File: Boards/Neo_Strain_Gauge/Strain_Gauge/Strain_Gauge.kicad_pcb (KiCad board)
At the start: 2 copper layers, 85 x 56 mm, 60 parts, among them J1 Screw_Terminal_01x03, J2 Screw_Terminal_01x03, J3 Screw_Terminal_01x03, J4 Screw_Terminal_01x03, J5 Conn_01x02, J6 USB_B_Micro, J7 Conn_02x10_Counter_Clockwise, J8 Conn_02x12_Counter_Clockwise, U1 W25Q128JVS, U2 NCP1117-3.3_SOT223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

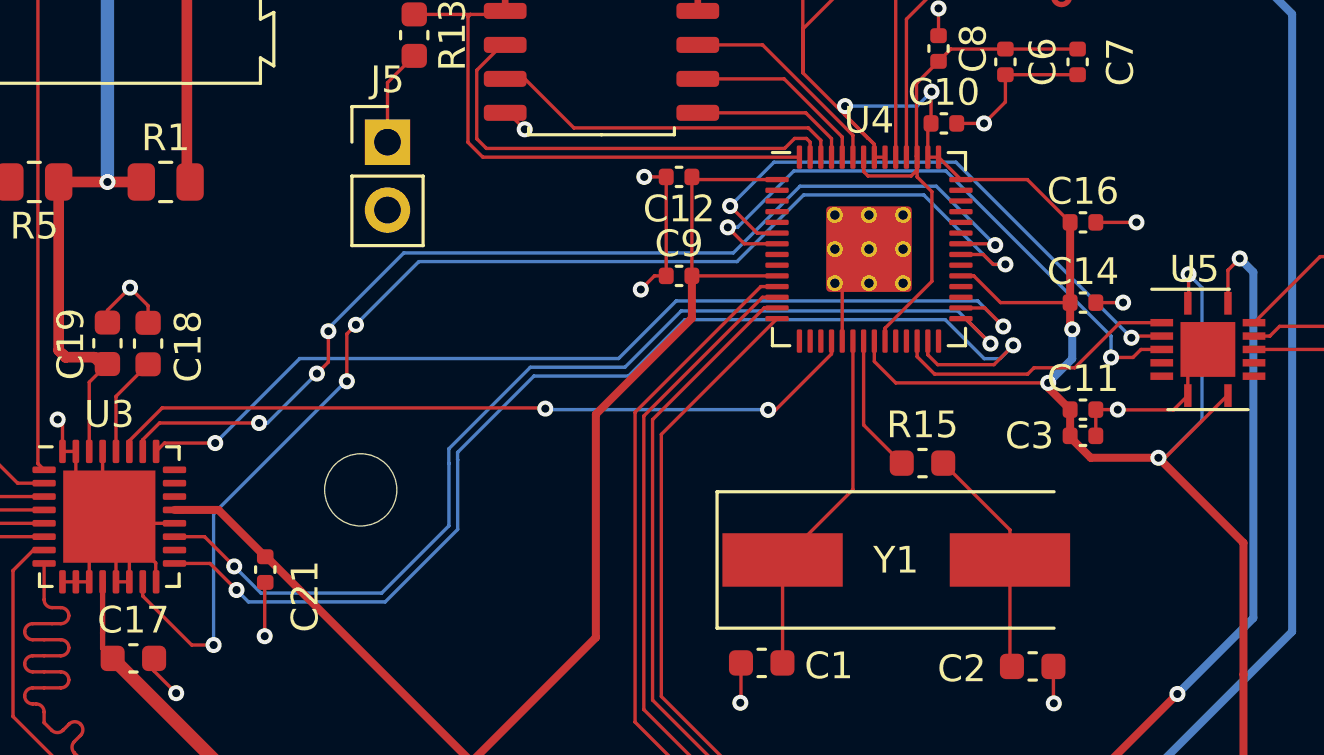
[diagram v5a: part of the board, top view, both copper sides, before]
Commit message: Swap what we use for the SPI pins to make routing slightly better
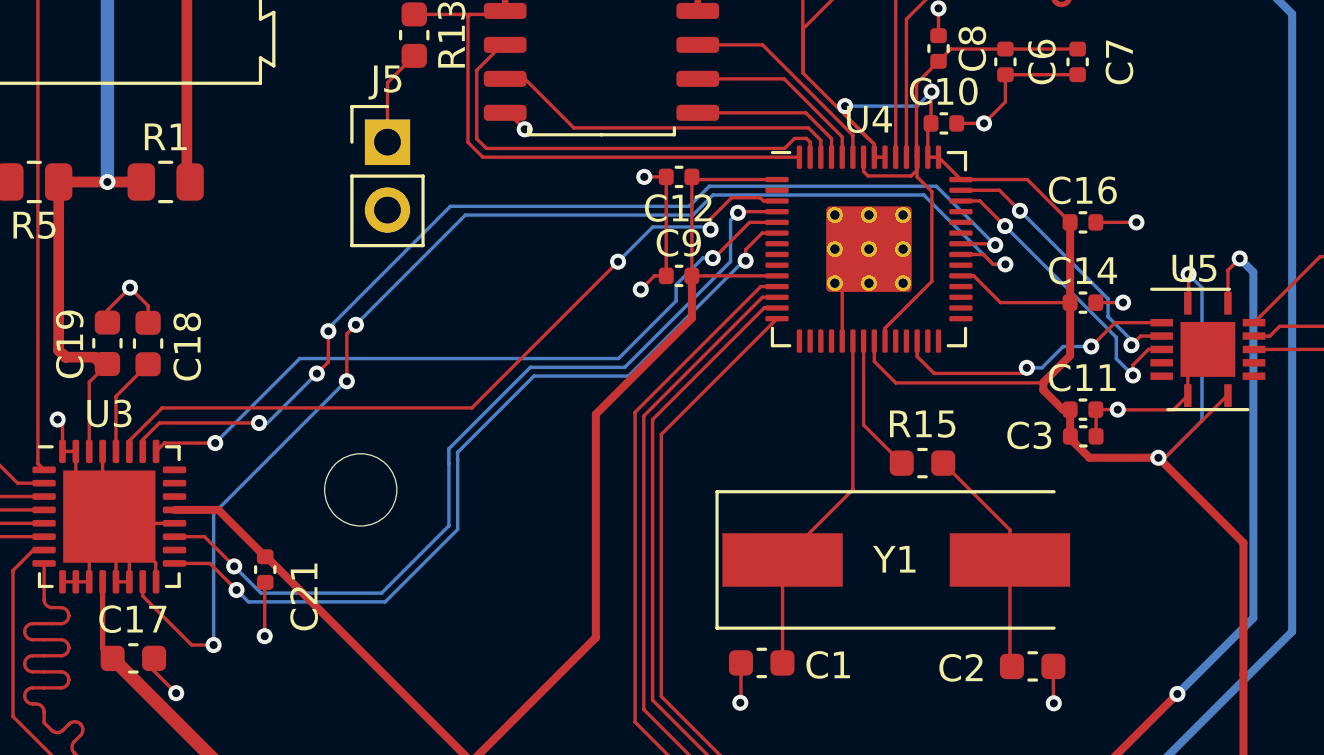
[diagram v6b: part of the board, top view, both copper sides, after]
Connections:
- U3 pad 17: /GPIO16 -> /GPIO4
- U3 pad 19: /GPIO18 -> /GPIO2
- U3 pad 25: /GPIO19 -> /GPIO3
- U3 pad 27: /GPIO15 -> /GPIO1
- U5 pad 3: /GPIO4 -> /GPIO29_ADC3
- U5 pad 4: /GPIO5 -> /GPIO28_ADC2
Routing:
- net /GPIO16: track 43.0 -> 0.00 mm, vias 2 -> 0
- net /GPIO18: track 39.4 -> 0.00 mm, vias 2 -> 0
- net /GPIO19: track 36.3 -> 0.00 mm, vias 2 -> 0
- net /GPIO2: track 0.00 -> 31.9 mm, vias 0 -> 2
- net /GPIO1: track 0.00 -> 28.8 mm, vias 0 -> 2
- net /GPIO15: track 28.5 -> 0.00 mm, vias 2 -> 0
- net /GPIO3: track 0.00 -> 27.1 mm, vias 0 -> 2
- net /GPIO5: track 22.7 -> 0.00 mm, vias 2 -> 0
- net /GPIO28_ADC2: track 0.00 -> 11.3 mm, vias 0 -> 2
- net /GPIO29_ADC3: track 0.00 -> 10.6 mm, vias 0 -> 2
- net /GPIO4: track 21.7 -> 30.8 mm
- net +3V3: track 192.2 -> 192.3 mm, vias 8 -> 6
- net /RUN: vias 0 -> 2

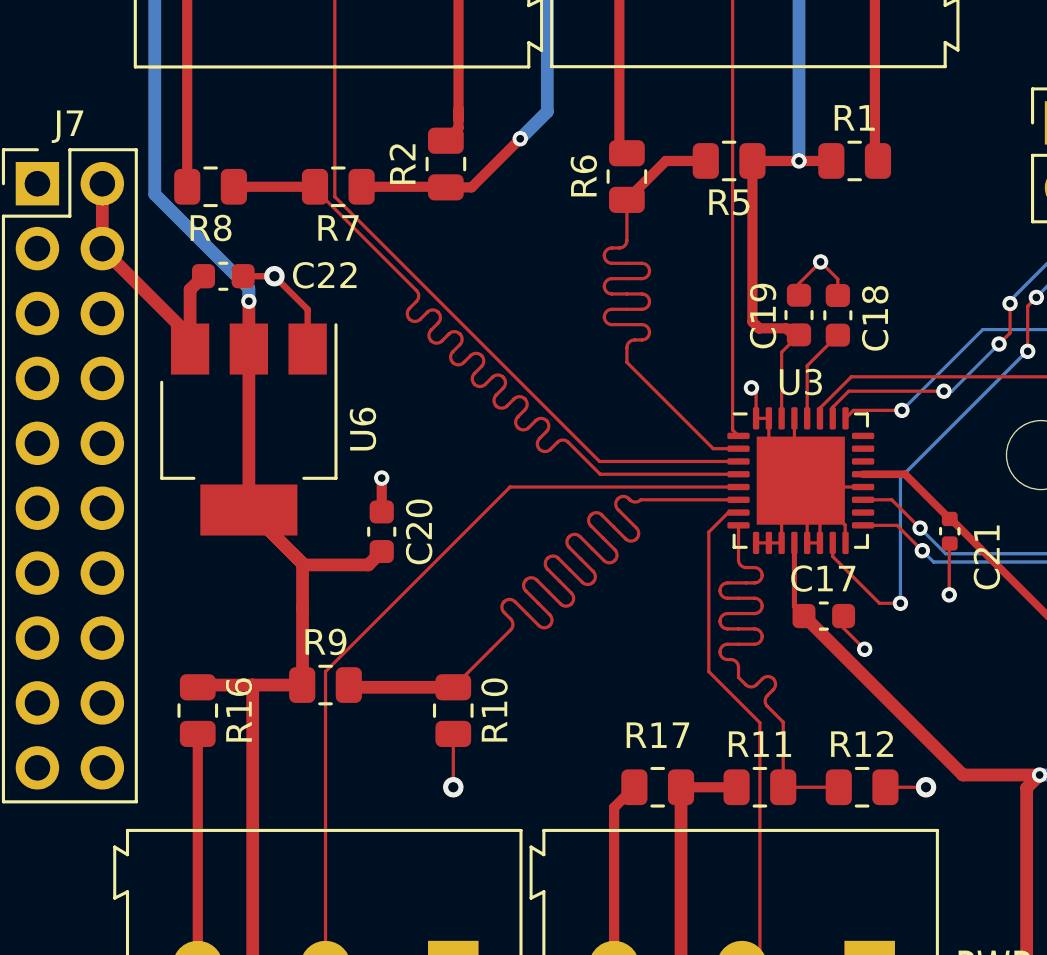
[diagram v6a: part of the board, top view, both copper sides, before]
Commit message: Filter the voltage input to the system
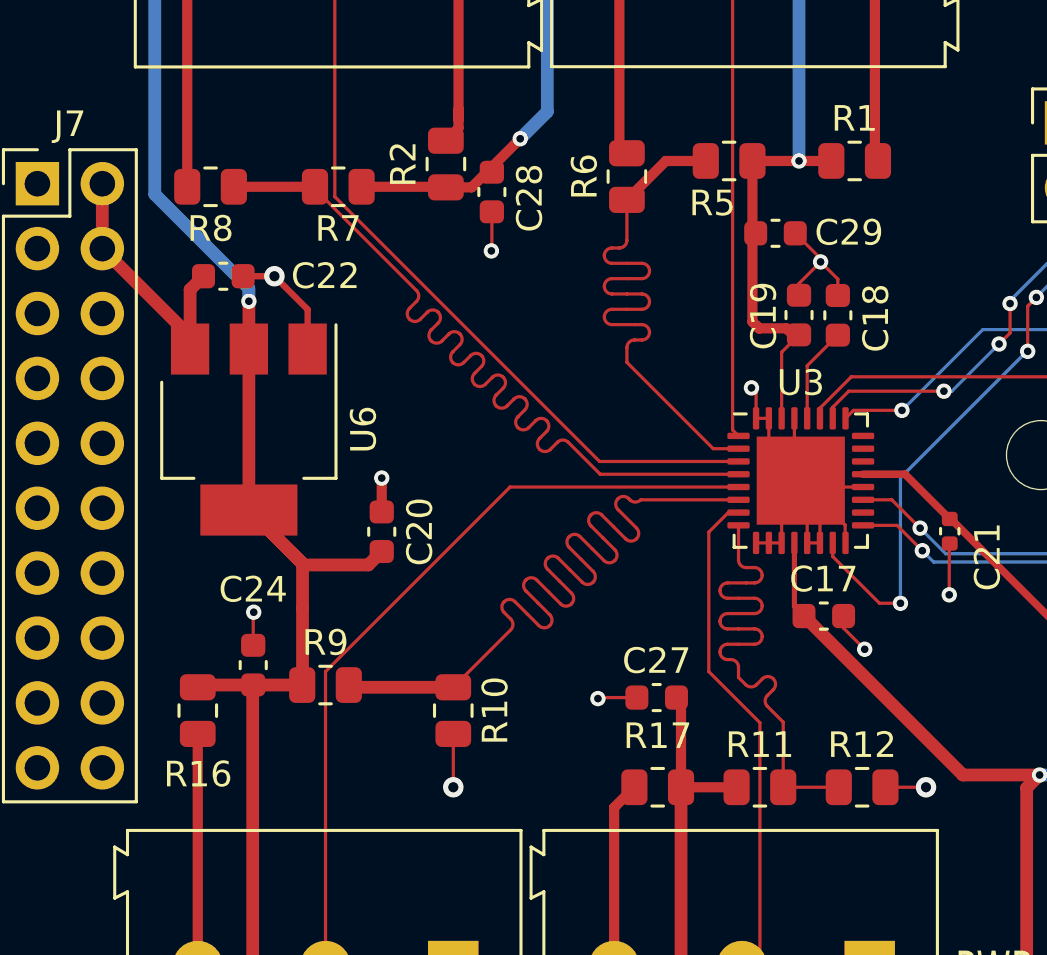
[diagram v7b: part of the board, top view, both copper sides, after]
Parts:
- added C24: 0.1pF, Capacitor_SMD:C_0603_1608Metric, F.Cu at (111.2, 90.2)
- added C27: 0.1pF, Capacitor_SMD:C_0603_1608Metric, F.Cu at (127.0, 91.5)
- added C28: 0.1pF, Capacitor_SMD:C_0603_1608Metric, F.Cu at (120.5, 71.7)
- added C29: 0.1pF, Capacitor_SMD:C_0603_1608Metric, F.Cu at (131.6, 73.3)
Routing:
- net GND: track 110.0 -> 115.9 mm, vias 21 -> 24
- net +5V: track 224.2 -> 227.7 mm

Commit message: Add test points to debug board communication
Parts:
- added TP1: TestPoint, TestPoint:TestPoint_THTPad_D1.0mm_Drill0.5mm, F.Cu at (147.6, 76.4)
- added TP2: TestPoint, TestPoint:TestPoint_THTPad_D1.0mm_Drill0.5mm, F.Cu at (138.3, 76.5)
- added TP3: TestPoint, TestPoint:TestPoint_THTPad_D1.0mm_Drill0.5mm, F.Cu at (144.6, 76.4)
- added TP4: TestPoint, TestPoint:TestPoint_THTPad_D1.0mm_Drill0.5mm, F.Cu at (147.5, 83.8)
- added TP5: TestPoint, TestPoint:TestPoint_THTPad_D1.0mm_Drill0.5mm, F.Cu at (149.2, 80.0)
- added TP6: TestPoint, TestPoint:TestPoint_THTPad_D1.0mm_Drill0.5mm, F.Cu at (170.9, 83.2)
- added TP7: TestPoint, TestPoint:TestPoint_THTPad_D1.0mm_Drill0.5mm, F.Cu at (171.4, 69.2)
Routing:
- net /GPIO29_ADC3: track 10.6 -> 16.3 mm
- net /GPIO2: track 31.9 -> 37.5 mm, vias 2 -> 3
- net /GPIO28_ADC2: track 11.3 -> 16.9 mm
- net /GPIO24: track 39.2 -> 42.8 mm
- net /GPIO1: track 28.8 -> 32.0 mm
- net /GPIO4: track 30.8 -> 33.4 mm
- net /GPIO3: track 27.1 -> 29.1 mm
- net GND: track 115.9 -> 115.0 mm, vias 24 -> 23
